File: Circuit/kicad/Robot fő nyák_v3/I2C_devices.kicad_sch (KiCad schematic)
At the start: 45 parts, among them J19 Conn_01x04_Pin, J20 Conn_01x04_Pin, J21 Conn_01x04_Pin, J23 Conn_01x04_Pin, J24 Conn_01x04_Pin, J25 Conn_01x04_Pin, J26 Conn_01x04_Pin, J27 Conn_01x04_Pin, J28 Conn_01x04_Pin, J29 Conn_01x04_Pin, J30 Conn_01x04_Pin, J31 Conn_01x04_Pin, J32 Conn_01x04_Pin, J33 Conn_01x04_Pin, J34 Conn_01x04_Pin, J35 Conn_01x04_Pin, Q10 IRLML2502, Q11 IRLML2502, Q12 IRLML2502, Q13 IRLML2502, Q14 IRLML2502, Q15 IRLML2502, Q16 IRLML2502, Q17 IRLML2502, Q18 IRLML2502, Q19 IRLML2502, Q4 IRLML2502, Q5 IRLML2502, Q6 IRLML2502, Q7 IRLML2502, Q8 IRLML2502, Q9 IRLML2502, SW2 SW_DIP_x08, U42 TCA9548APWR, U43 TCA9548APWR, U44 74HC240

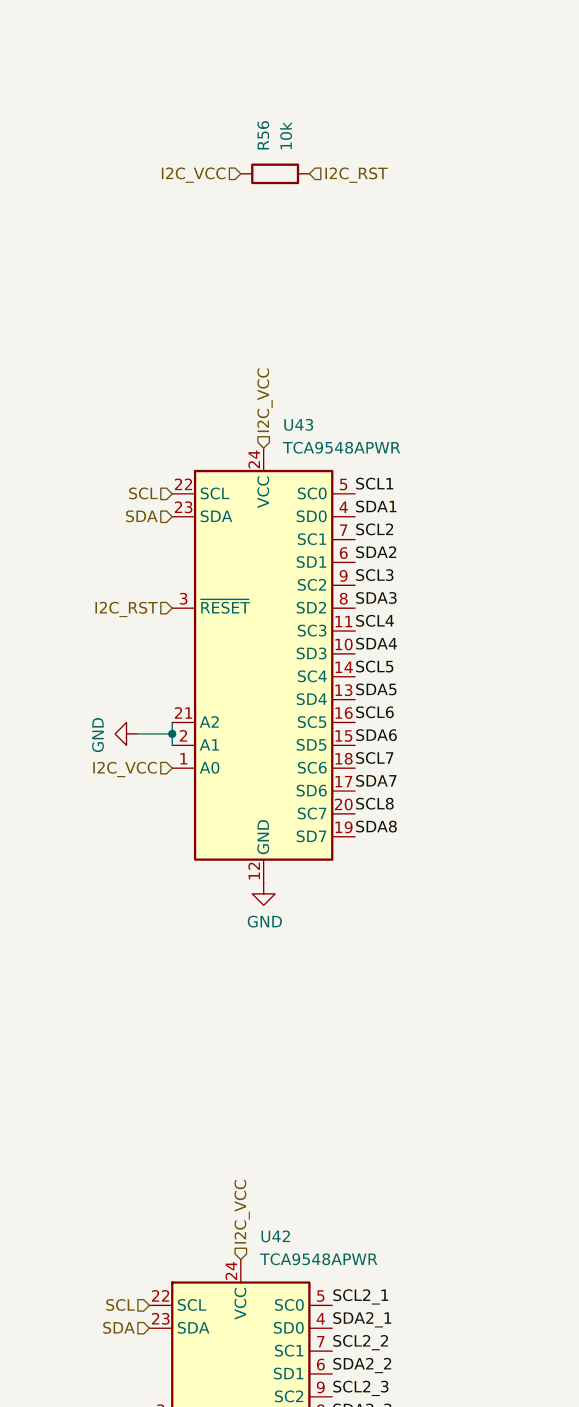
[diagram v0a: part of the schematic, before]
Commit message: KICAD V3.01 Cleaned sheets + update + szekér modell add
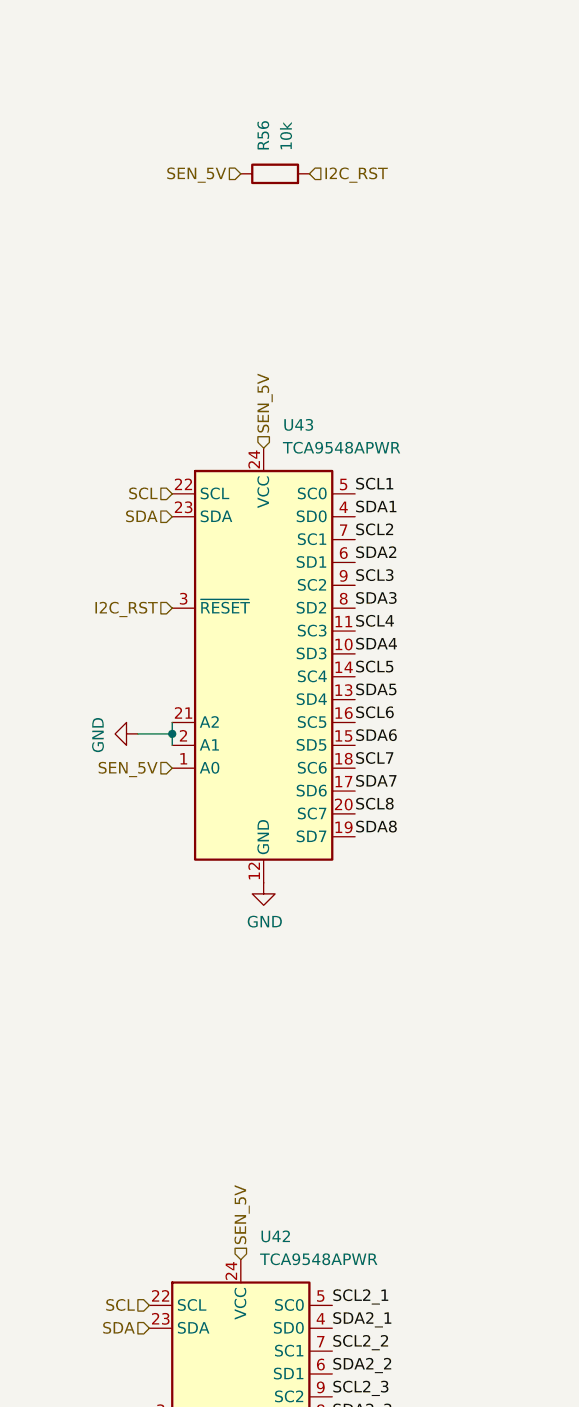
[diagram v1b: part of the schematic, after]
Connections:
- net I2C_VCC is gone; now on net SEN_5V: R56.1, U42.24 (VCC), U43.1 (A0), U43.24 (VCC)
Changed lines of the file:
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@@
 		)
 	)
-	(hierarchical_label "I2C_VCC"
+	(hierarchical_label "SEN_5V"
 		(shape input)
-		(at 53.34 201.93 90)
+		(at 53.34 81.28 180)
 		(effects
 			(font
 				(size 1.27 1.27)
 			)
-			(justify left)
+			(justify right)
 		)
 	)
@@
 		)
 	)
+	(hierarchical_label "SEN_5V"
+		(shape input)
+		(at 53.34 201.93 90)
+		(effects
+			(font
+				(size 1.27 1.27)
+			)
+			(justify left)
+		)
+	)
 	(hierarchical_label "SEN_3V3"
 		(shape input)
@@
 		)
 	)
-	(hierarchical_label "I2C_VCC"
+	(hierarchical_label "SCL"
 		(shape input)
-		(at 45.72 147.32 180)
+		(at 43.18 207.01 180)
 		(effects
 			(font
@@
 		)
 	)
-	(hierarchical_label "SCL"
+	(hierarchical_label "SEN_5V"
 		(shape input)
-		(at 43.18 207.01 180)
+		(at 45.72 147.32 180)
 		(effects
 			(font
@@
 		)
 	)
-	(hierarchical_label "I2C_VCC"
-		(shape input)
-		(at 53.34 81.28 180)
-		(effects
-			(font
-				(size 1.27 1.27)
-			)
-			(justify right)
-		)
-	)
 	(hierarchical_label "SCL"
 		(shape input)
@@
 		)
 	)
-	(hierarchical_label "I2C_VCC"
+	(hierarchical_label "SEN_5V"
 		(shape input)
 		(at 55.88 111.76 90)

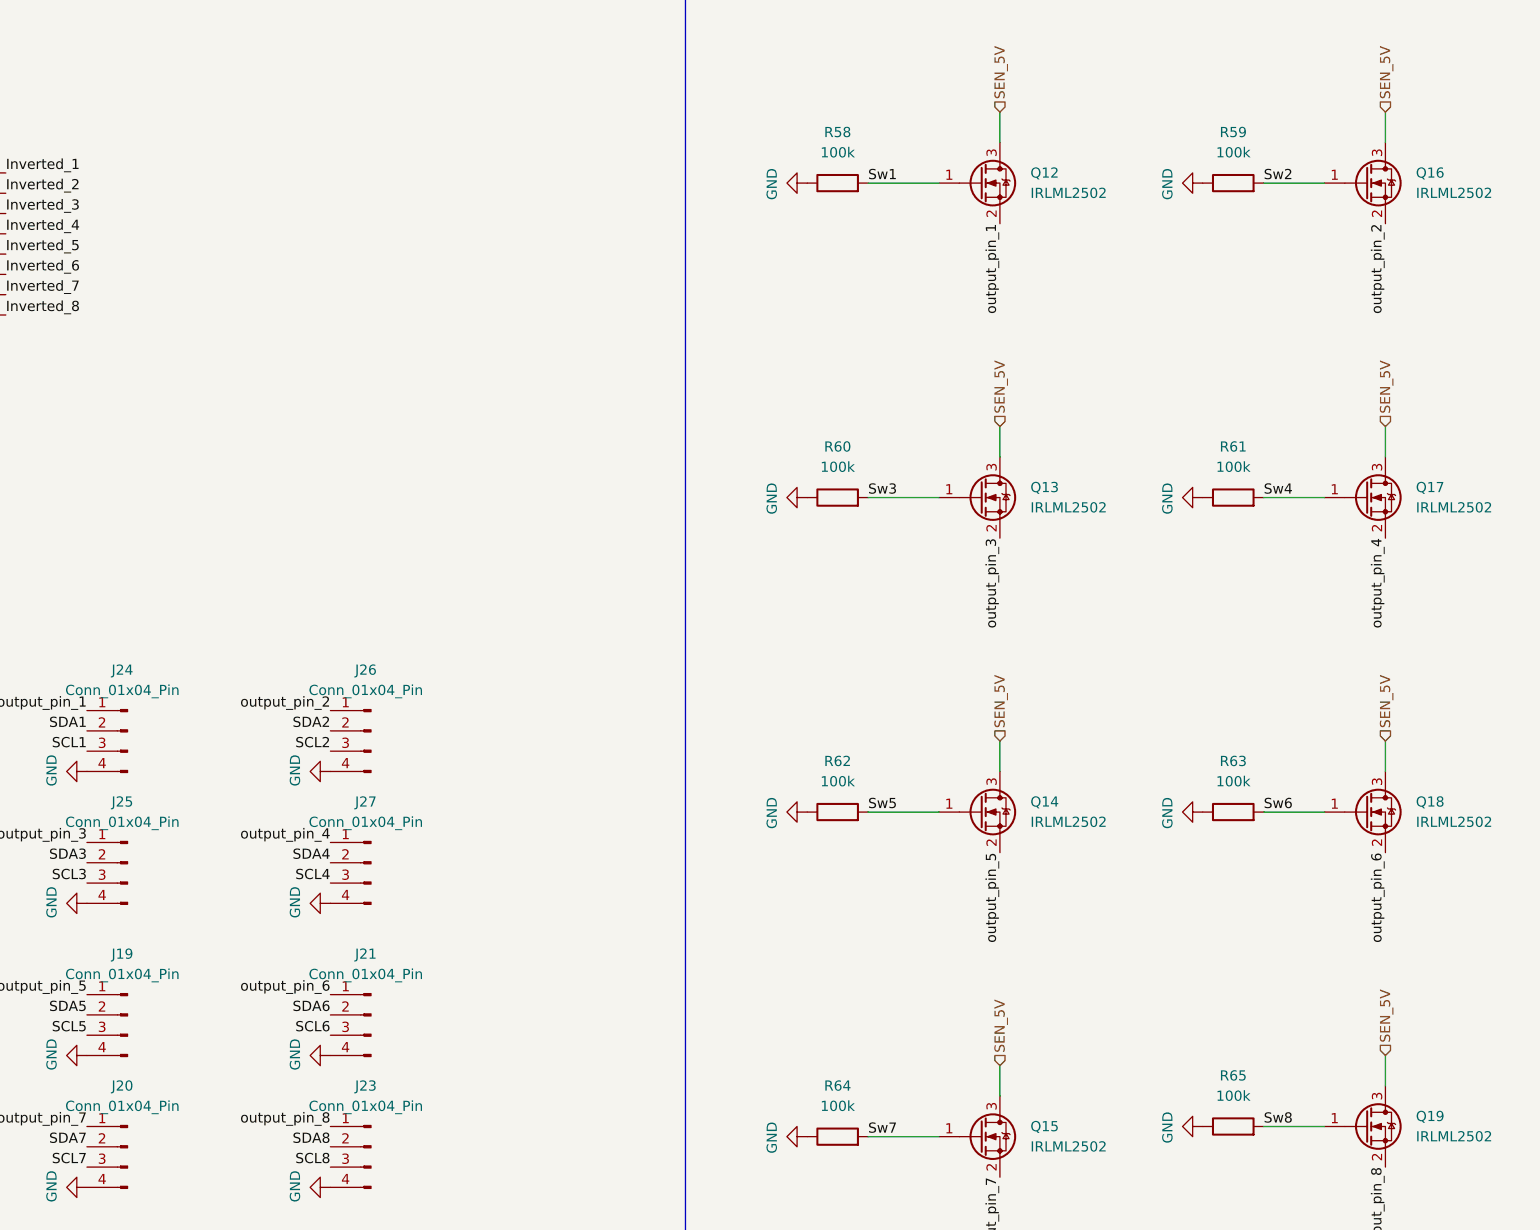
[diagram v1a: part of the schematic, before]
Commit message: Kicad update: power rails v1.0, todo: hc-sr-04  as6500 ic review shift registers change to MCP23S17_SO
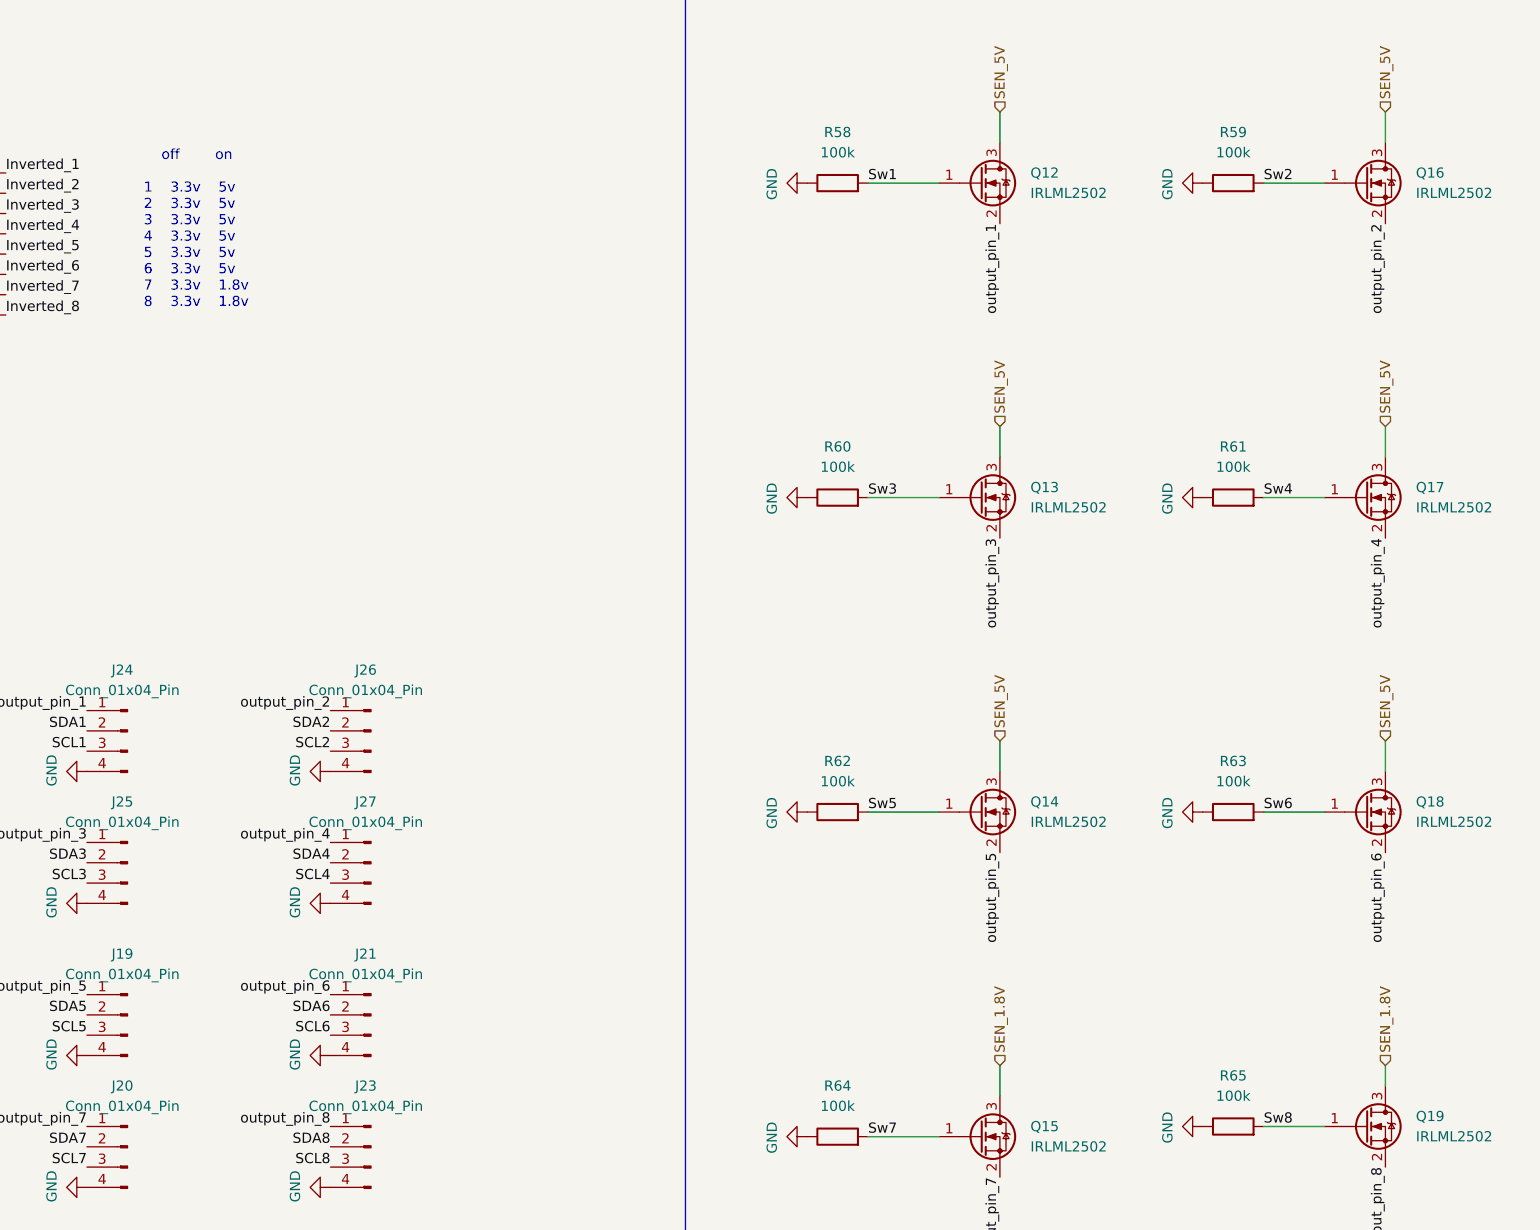
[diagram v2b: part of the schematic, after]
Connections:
- net SEN_5V: no longer Q15.3 (D), Q19.3 (D)
- new net SEN_1.8V: Q15.3 (D), Q19.3 (D)
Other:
- note added: "off on 1 3.3v 5v 2 3.3v 5v 3 3.3v 5v 4 3.3v 5v 5 3.3v 5v 6 3.3v 5v 7 3.3v 1.8v 8 3.3v 1.8v"
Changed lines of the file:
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@@
 	(generator_version "9.0")
 	(paper "A3")
+	(text "	off		on	\n\n1	3.3v	5v\n2	3.3v	5v\n3	3.3v	5v\n4	3.3v	5v\n5	3.3v	5v\n6	3.3v	5v\n7	3.3v	1.8v\n8	3.3v	1.8v\n"
+		(exclude_from_sim no)
+		(at 144.272 47.752 0)
+		(effects
+			(font
+				(size 1.27 1.27)
+			)
+			(justify left)
+		)
+	)
 	(text_box "Átkapcsoló mosfetek"
 		(exclude_from_sim no)
@@
 	(wire
 		(pts
-			(xy 299.72 151.13) (xy 299.72 154.94)
-		)
-		(stroke
-			(width 0)
-			(type default)
-		)
-	)
-	(wire
-		(pts
 			(xy 86.36 48.26) (xy 101.6 48.26)
 		)
@@
 		(pts
 			(xy 43.18 234.95) (xy 43.18 237.49)
+		)
+		(stroke
+			(width 0)
+			(type default)
+		)
+	)
+	(wire
+		(pts
+			(xy 299.72 152.4) (xy 299.72 154.94)
 		)
 		(stroke
@@
 		)
 	)
+	(hierarchical_label "SEN_1.8V"
+		(shape input)
+		(at 299.72 152.4 90)
+		(effects
+			(font
+				(size 1.27 1.27)
+			)
+			(justify left)
+		)
+	)
 	(hierarchical_label "SEN_3V3"
 		(shape input)
@@
 		)
 	)
+	(hierarchical_label "SEN_1.8V"
+		(shape input)
+		(at 251.46 152.4 90)
+		(effects
+			(font
+				(size 1.27 1.27)
+			)
+			(justify left)
+		)
+	)
 	(hierarchical_label "SEN_5V"
 		(shape input)
@@
 		)
 	)
+	(hierarchical_label "I2C_RST"
+		(shape input)
+		(at 43.18 219.71 180)
+		(effects
+			(font
+				(size 1.27 1.27)
+			)
+			(justify right)
+		)
+	)
 	(hierarchical_label "SEN_5V"
 		(shape input)
-		(at 299.72 151.13 90)
+		(at 53.34 201.93 90)
 		(effects
 			(font
@@
 		)
 	)
-	(hierarchical_label "I2C_RST"
-		(shape input)
-		(at 43.18 219.71 180)
+	(hierarchical_label "SEN_3V3"
+		(shape input)
+		(at 378.46 33.02 90)
+		(effects
+			(font
+				(size 1.27 1.27)
+			)
+			(justify left)
+		)
+	)
+	(hierarchical_label "SCL"
+		(shape input)
+		(at 43.18 207.01 180)
 		(effects
 			(font
@@
 	(hierarchical_label "SEN_5V"
 		(shape input)
-		(at 53.34 201.93 90)
+		(at 45.72 147.32 180)
+		(effects
+			(font
+				(size 1.27 1.27)
+			)
+			(justify right)
+		)
+	)
+	(hierarchical_label "SEN_5V"
+		(shape input)
+		(at 251.46 72.39 90)
 		(effects
 			(font
@@
 		)
 	)
+	(hierarchical_label "SEN_5V"
+		(shape input)
+		(at 251.46 33.02 90)
+		(effects
+			(font
+				(size 1.27 1.27)
+			)
+			(justify left)
+		)
+	)
+	(hierarchical_label "SEN_5V"
+		(shape input)
+		(at 66.04 31.75 180)
+		(effects
+			(font
+				(size 1.27 1.27)
+			)
+			(justify right)
+		)
+	)
 	(hierarchical_label "SEN_3V3"
 		(shape input)
-		(at 378.46 33.02 90)
+		(at 340.36 152.4 90)
 		(effects
 			(font
@@
 		)
 	)
+	(hierarchical_label "SEN_5V"
+		(shape input)
+		(at 299.72 111.76 90)
+		(effects
+			(font
+				(size 1.27 1.27)
+			)
+			(justify left)
+		)
+	)
 	(hierarchical_label "SCL"
 		(shape input)
-		(at 43.18 207.01 180)
+		(at 45.72 116.84 180)
 		(effects
 			(font
@@
 	(hierarchical_label "SEN_5V"
 		(shape input)
-		(at 45.72 147.32 180)
-		(effects
-			(font
-				(size 1.27 1.27)
-			)
-			(justify right)
-		)
-	)
-	(hierarchical_label "SEN_5V"
-		(shape input)
-		(at 251.46 72.39 90)
+		(at 55.88 111.76 90)
 		(effects
 			(font
@@
 		)
 	)
-	(hierarchical_label "SEN_5V"
-		(shape input)
-		(at 251.46 33.02 90)
-		(effects
-			(font
-				(size 1.27 1.27)
-			)
-			(justify left)
-		)
-	)
-	(hierarchical_label "SEN_5V"
-		(shape input)
-		(at 66.04 31.75 180)
-		(effects
-			(font
-				(size 1.27 1.27)
-			)
-			(justify right)
-		)
-	)
 	(hierarchical_label "SEN_3V3"
 		(shape input)
-		(at 340.36 152.4 90)
-		(effects
-			(font
-				(size 1.27 1.27)
-			)
-			(justify left)
-		)
-	)
-	(hierarchical_label "SEN_5V"
-		(shape input)
-		(at 299.72 111.76 90)
-		(effects
-			(font
-				(size 1.27 1.27)
-			)
-			(justify left)
-		)
-	)
-	(hierarchical_label "SCL"
-		(shape input)
-		(at 45.72 116.84 180)
-		(effects
-			(font
-				(size 1.27 1.27)
-			)
-			(justify right)
-		)
-	)
-	(hierarchical_label "SEN_5V"
-		(shape input)
-		(at 55.88 111.76 90)
-		(effects
-			(font
-				(size 1.27 1.27)
-			)
-			(justify left)
-		)
-	)
-	(hierarchical_label "SEN_3V3"
-		(shape input)
 		(at 340.36 72.39 90)
 		(effects
 			(font
-				(size 1.27 1.27)
-			)
-			(justify left)
-		)
-	)
-	(hierarchical_label "SEN_5V"
-		(shape input)
-		(at 251.46 152.4 90)
-		(effects
-			(font
